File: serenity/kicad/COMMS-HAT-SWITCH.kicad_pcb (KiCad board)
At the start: 4 copper layers, 65 x 52 mm, 39 parts, among them Y1 25MHz-XTAL

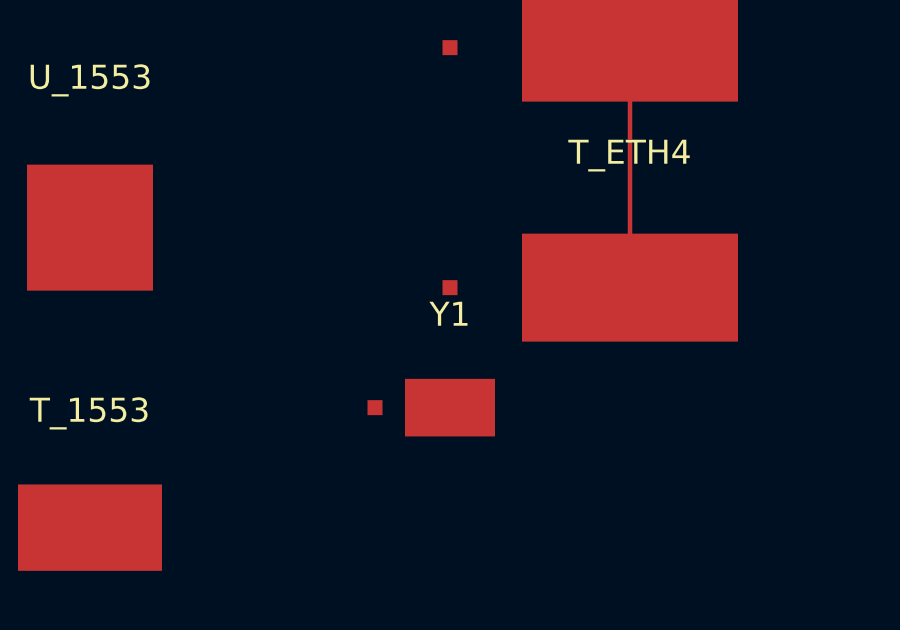
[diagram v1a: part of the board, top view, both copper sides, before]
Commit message: Replace generic PCB silk labels with short descriptive names
Update all F.SilkS/B.SilkS fp_text reference labels across 7 KiCad PCB
files, replacing J/U/T numeric designators with function-based names so
each component is identifiable on the board without a BOM lookup.

CAPE-A-1 / CAPE-A-1-no-comment:
  J1→PB2-P1, J2→PB2-P2, U1→IMU, U2→BARO, U3→GPS,
  U4/U5→CAN-TR/RS485, U6→1553-DRV, U7→1553-RCV, T1→1553-XFM,
  U8/U9→ETH1-PHY/ETH2-PHY, U10→TPM,
  J3→CAN-FD, J4→RS-485, J5→MIL-1553, J6→ETH1, J7→ETH2,
  J8→ESC-TLM, J9→SERVO, J10→PWR-IN

CAPE-B-1 (adds RF + payload peripherals):
  U1→LORA, U2→WIFI-BT, U10→SD-WB, U11→NOR-FLASH,
  U12→WINCH-DRV, U13→LOAD-ADC, U14→PWM-I2C,
  J8→SIK-TLM, J9→RC-RCVR, J11→WINCH, J12→LOAD-CELL, J13→NAV-LIGHT

COMMS-HAT-1 (connectors + crystal only; ICs already descriptive):
  J1→SIK-UART, J2→ETH, J3→GPIO-EXT, J4→CAN-FD,
  JP4→PWR-IN, Y1→ETH-CLK

COMMS-HAT-SWITCH:
  Y1→SW-CLK

TRIHAT-1 (superseded; ICs + inferred connector mapping):
  U1→IMU, U2→BARO, U3→GPS, U4→CAN-CTRL, U5→CAN-TR,
  U6→ETH-CTRL, U7→ETH-MAG, U8→TPM, U9→LDO, Y1→ETH-CLK,
  J-connectors mapped from net list (GPS/CAN-FD/ETH/ESC-OUT/SERVO-OUT/etc.)

CM3-CARRIER-1:
  J1→CM3-SDIMM, U1→CAN-CTRL, U1B→CAN-TR, U2→RS485,
  U3→MIL-1553, U4→ETH-CTRL, U5→USB-UART, U6→LDO, U7→HAT-EEPROM

Boards already fully descriptive (SENSORHAT-1, CM4-CARRIER-1,
CM4-CARRIER-2) are unchanged.

https://claude.ai/code/session_01GniMw4QukTVM7JMzyVjH6p
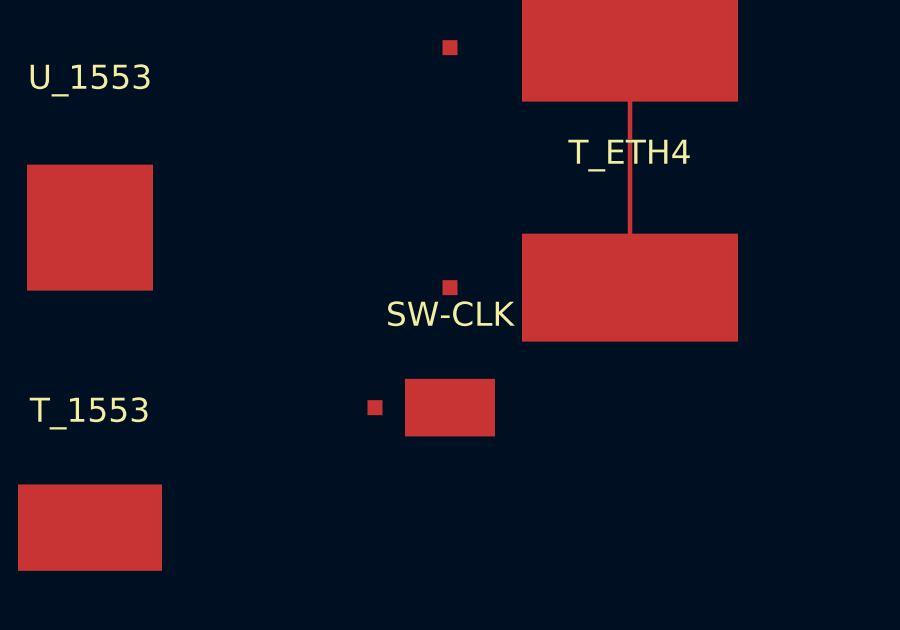
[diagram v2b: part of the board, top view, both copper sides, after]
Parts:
- removed Y1: 25MHz-XTAL, Package
- added SW-CLK: 25MHz-XTAL, Package, F.Cu at (20.0, 44.0)
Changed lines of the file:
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@@
     (pad "EP" smd rect (at 0 0) (size 1.80 1.20) (layers "F.Cu" "F.Paste" "F.Mask")))
   (footprint "Package" (layer "F.Cu") (at 20 44) (property "Description" "KSZ8895 reference clock SMD")
-    (fp_text reference "Y1" (at 0 -3.1) (layer "F.SilkS")
+    (fp_text reference "SW-CLK" (at 0 -3.1) (layer "F.SilkS")
       (effects (font (size 0.8 0.8) (thickness 0.15))))
     (fp_text value "25MHz-XTAL" (at 0 3.1) (layer "F.Fab")
